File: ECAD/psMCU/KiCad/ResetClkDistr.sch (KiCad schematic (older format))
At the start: 2 parts, among them U35 SN74HC245PW

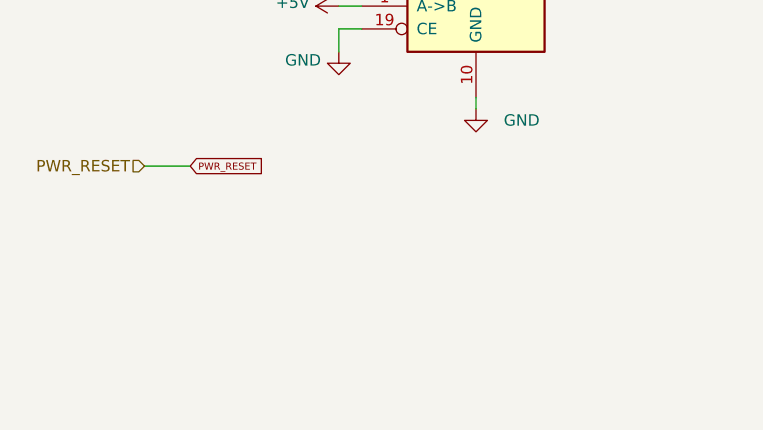
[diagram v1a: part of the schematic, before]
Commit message: Sch: Implemented much improved debugger interface
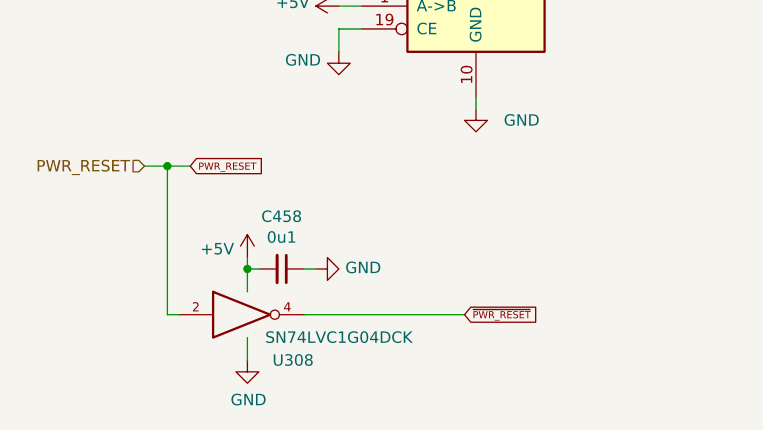
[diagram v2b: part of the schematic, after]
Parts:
- added C458: 0u1, NoRef_Footprints:C_0603_1608Metric_NoRef, symbol Device:C_Small
- added U308: SN74LVC1G04DCK, Package_TO_SOT_SMD:SOT-353_SC-70-5, symbol 74xGxx:74LVC1G04
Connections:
- net +5V: now also C458.2, U308.5 (VCC)
- net GND: now also C458.1, U308.3 (GND)
- net PWR_RESET: now also U308.2
- new net ~PWR_RESET: U308.4
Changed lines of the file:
@@
 $Descr A4 11693 8268
 encoding utf-8
-Sheet 95 102
+Sheet 86 105
 Title ""
 Date ""
@@
 PWR_RESET
 Wire Wire Line
-	4300 3150 4100 3150
+	4300 3150 4200 3150
 Text GLabel 4450 2050 2    31   Input ~ 0
 CLK
@@
 Wire Wire Line
 	4250 1550 4950 1550
+$Comp
+L 74xGxx:74LVC1G04 U?
+U 1 1 6512BE99
+P 4550 3800
+AR Path="/5ED2705B/6512BE99" Ref="U?"  Part="1"
+AR Path="/5F1CE57C/6512BE99" Ref="U?"  Part="1"
+AR Path="/5F607AA2/6512BE99" Ref="U?"  Part="1"
+AR Path="/5FD6F3D6/6512BE99" Ref="U?"  Part="1"
+AR Path="/62B3D95F/6512BE99" Ref="U308"  Part="1"
+F 0 "U308" H 4750 3600 50  0000 C CNN
+F 1 "SN74LVC1G04DCK" H 4950 3700 50  0000 C CNN
+F 2 "Package_TO_SOT_SMD:SOT-353_SC-70-5" H 4550 3800 50  0001 C CNN
+F 3 "http://www.ti.com/lit/sg/scyt129e/scyt129e.pdf" H 4550 3800 50  0001 C CNN
+	1    4550 3800
+	1    0    0    -1
+$EndComp
+Wire Wire Line
+	4550 3700 4550 3600
+$Comp
+L power:+5V #PWR?
+U 1 1 6512BEA0
+P 4550 3550
+AR Path="/5ED2705B/6512BEA0" Ref="#PWR?"  Part="1"
+AR Path="/5F1CE57C/6512BEA0" Ref="#PWR?"  Part="1"
+AR Path="/5F607AA2/6512BEA0" Ref="#PWR?"  Part="1"
+AR Path="/5FD6F3D6/6512BEA0" Ref="#PWR?"  Part="1"
+AR Path="/62B3D95F/6512BEA0" Ref="#PWR01731"  Part="1"
+F 0 "#PWR01731" H 4550 3400 50  0001 C CNN
+F 1 "+5V" H 4492 3587 50  0000 R CNN
+F 2 "" H 4550 3550 50  0001 C CNN
+F 3 "" H 4550 3550 50  0001 C CNN
+	1    4550 3550
+	1    0    0    -1
+$EndComp
+$Comp
+L Device:C_Small C?
+U 1 1 6512BEA6
+P 4700 3600
+AR Path="/5ED2705B/6512BEA6" Ref="C?"  Part="1"
+AR Path="/5F1CE57C/6512BEA6" Ref="C?"  Part="1"
+AR Path="/5F607AA2/6512BEA6" Ref="C?"  Part="1"
+AR Path="/5FD6F3D6/6512BEA6" Ref="C?"  Part="1"
+AR Path="/62B3D95F/6512BEA6" Ref="C458"  Part="1"
+F 0 "C458" V 4471 3600 50  0000 C CNN
+F 1 "0u1" V 4562 3600 50  0000 C CNN
+F 2 "NoRef_Footprints:C_0603_1608Metric_NoRef" H 4700 3600 50  0001 C CNN
+F 3 "~" H 4700 3600 50  0001 C CNN
+	1    4700 3600
+	0    1    1    0
+$EndComp
+Wire Wire Line
+	4600 3600 4550 3600
+Connection ~ 4550 3600
+Wire Wire Line
+	4550 3600 4550 3550
+$Comp
+L power:GND #PWR?
+U 1 1 6512BEAF
+P 4850 3600
+AR Path="/5ED2705B/6512BEAF" Ref="#PWR?"  Part="1"
+AR Path="/5F1CE57C/6512BEAF" Ref="#PWR?"  Part="1"
+AR Path="/5F607AA2/6512BEAF" Ref="#PWR?"  Part="1"
+AR Path="/5FD6F3D6/6512BEAF" Ref="#PWR?"  Part="1"
+AR Path="/62B3D95F/6512BEAF" Ref="#PWR01733"  Part="1"
+F 0 "#PWR01733" H 4850 3350 50  0001 C CNN
+F 1 "GND" V 4855 3472 50  0000 R CNN
+F 2 "" H 4850 3600 50  0001 C CNN
+F 3 "" H 4850 3600 50  0001 C CNN
+	1    4850 3600
+	0    -1   -1   0
+$EndComp
+Wire Wire Line
+	4850 3600 4800 3600
+$Comp
+L power:GND #PWR?
+U 1 1 6512BEB6
+P 4550 4000
+AR Path="/5ED2705B/6512BEB6" Ref="#PWR?"  Part="1"
+AR Path="/5F1CE57C/6512BEB6" Ref="#PWR?"  Part="1"
+AR Path="/5F607AA2/6512BEB6" Ref="#PWR?"  Part="1"
+AR Path="/5FD6F3D6/6512BEB6" Ref="#PWR?"  Part="1"
+AR Path="/62B3D95F/6512BEB6" Ref="#PWR01732"  Part="1"
+F 0 "#PWR01732" H 4550 3750 50  0001 C CNN
+F 1 "GND" H 4555 3827 50  0000 C CNN
+F 2 "" H 4550 4000 50  0001 C CNN
+F 3 "" H 4550 4000 50  0001 C CNN
+	1    4550 4000
+	1    0    0    -1
+$EndComp
+Wire Wire Line
+	4550 4000 4550 3900
+Wire Wire Line
+	4800 3800 5500 3800
+Wire Wire Line
+	4250 3800 4200 3800
+Text GLabel 5500 3800 2    31   Input ~ 0
+~PWR_RESET
+Wire Wire Line
+	4200 3800 4200 3150
+Connection ~ 4200 3150
+Wire Wire Line
+	4200 3150 4100 3150
 $EndSCHEMATC

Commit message: Sch: Cleanup + Small fixes
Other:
- moved on the sheet: C251, C458, U308, U35

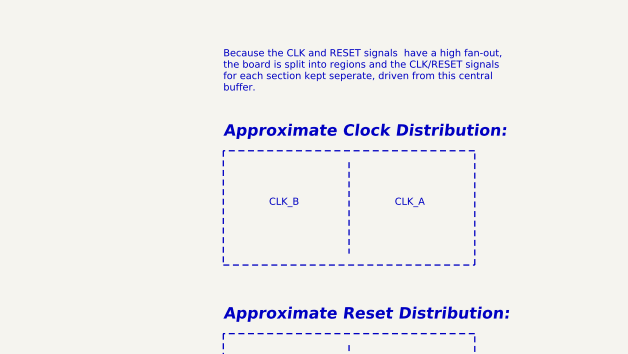
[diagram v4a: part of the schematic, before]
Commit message: Sch: More cleanup, fixed page descriptions.
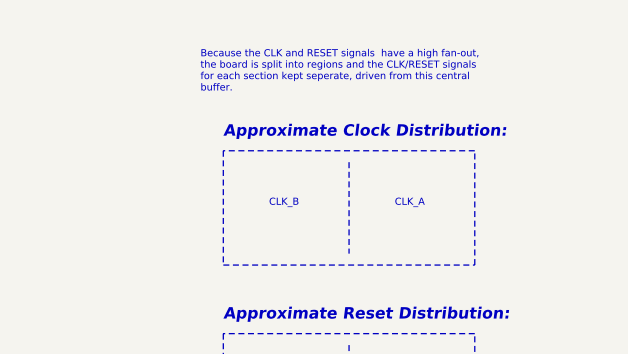
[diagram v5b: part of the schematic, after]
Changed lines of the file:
@@
 encoding utf-8
 Sheet 85 109
-Title ""
-Date ""
-Rev ""
-Comp ""
+Title "psMCU"
+Date "2022-02-20"
+Rev "v1.1"
+Comp "Philipp Schilk"
 Comment1 ""
 Comment2 ""
 Comment3 ""
-Comment4 ""
+Comment4 "Reset and clock signal distribution."
 $EndDescr
 Text HLabel 4250 2000 0    50   Input ~ 0
@@
 Wire Wire Line
 	4400 2200 4950 2200
-Text Notes 8650 1650 0    31   ~ 0
+Text Notes 8550 1650 0    31   ~ 0
 Because the CLK and RESET signals  have a high fan-out, \nthe board is split into regions and the CLK/RESET signals \nfor each section kept seperate, driven from this central\nbuffer.
 Text GLabel 4450 2300 2    31   Input ~ 0
